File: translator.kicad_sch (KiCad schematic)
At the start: 1 part, among them U1 STM32G071K8UxN

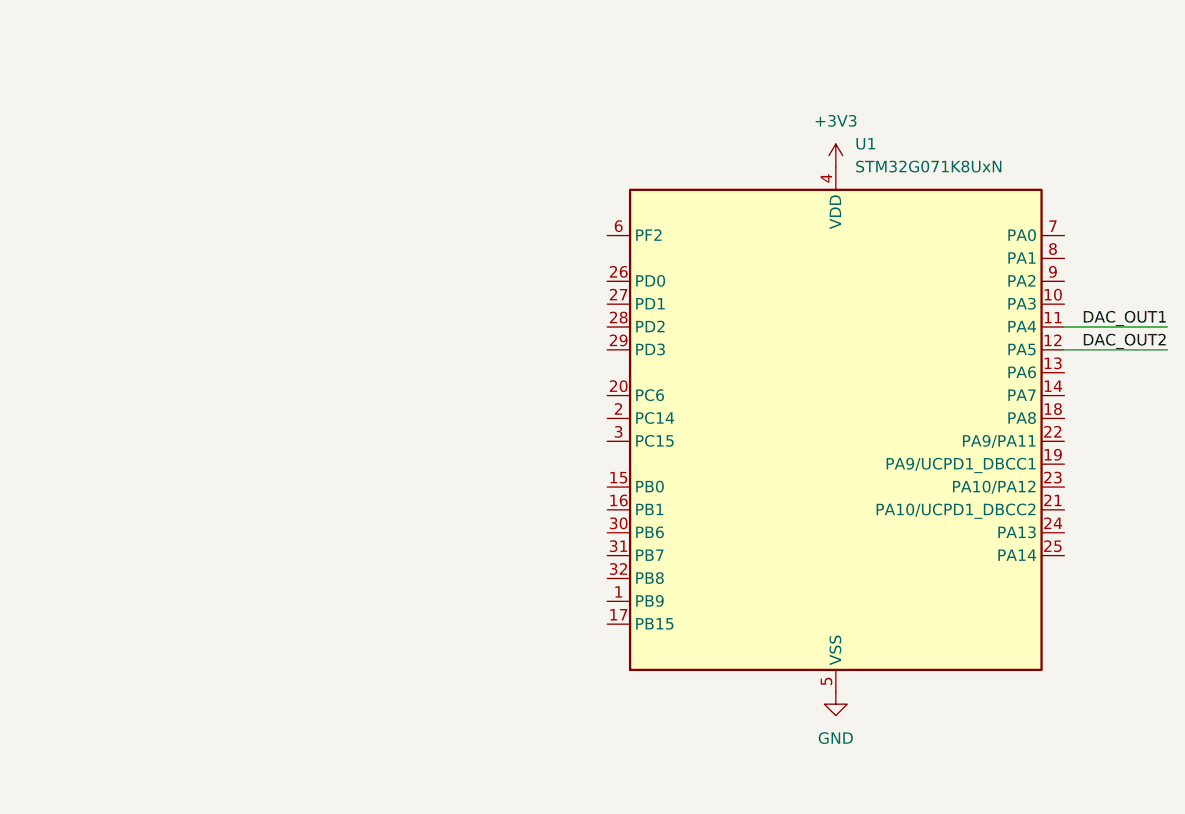
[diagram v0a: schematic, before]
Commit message: add schematic and pedal pinout
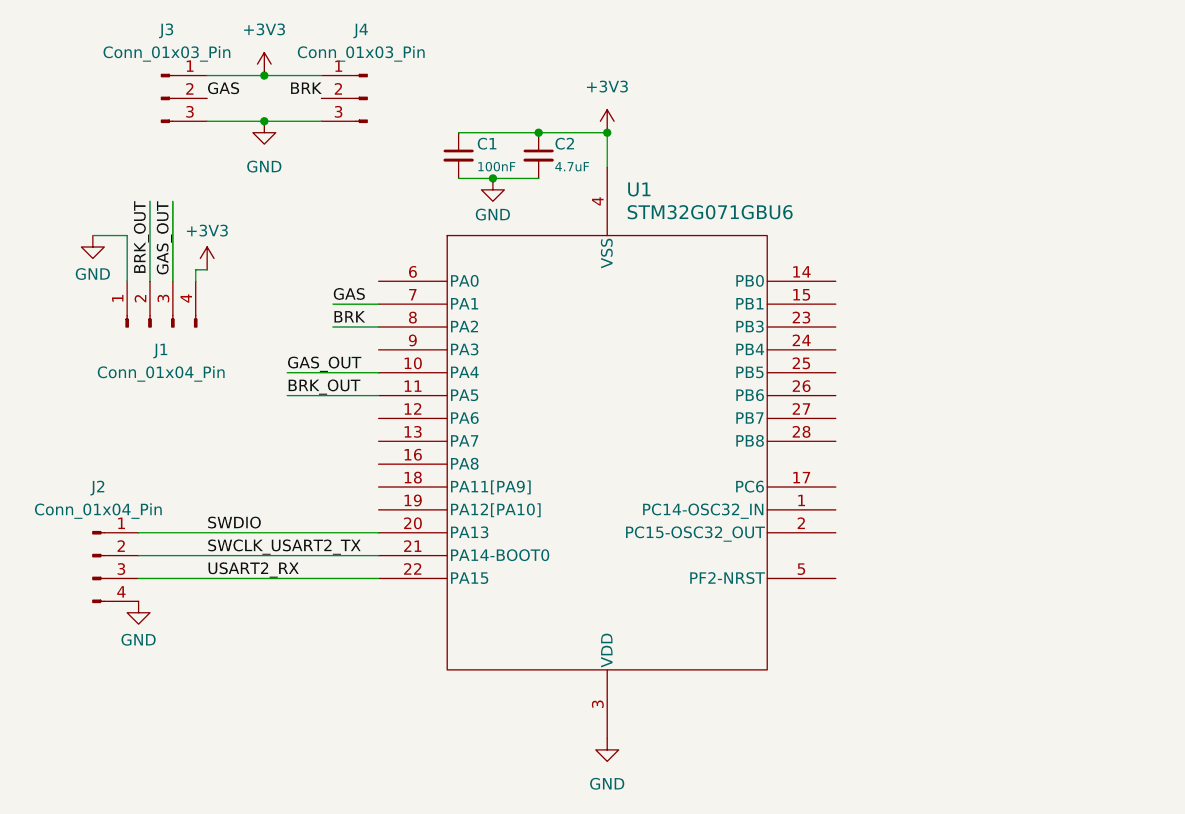
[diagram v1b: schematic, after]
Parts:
- removed U1: STM32G071K8UxN, Package_DFN_QFN:QFN-32-1EP_5x5mm_P0.5mm_EP3.45x3.45mm, symbol MCU_ST_STM32G0:STM32G071K8UxN
- added C1: 100nF, symbol Device:C_Small
- added C2: 4.7uF, symbol Device:C_Small
- added J1, J2: Conn_01x04_Pin, symbol Connector:Conn_01x04_Pin
- added J3, J4: Conn_01x03_Pin, symbol Connector:Conn_01x03_Pin
- added U1: STM32G071GBU6, translator:UFQFPN-28, symbol translator:STM32G071GBU6
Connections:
- net +3V3: now also C1.1, C2.1, J1.4 (Pin_4), J3.1 (Pin_1), J4.1 (Pin_1), U1.4 (VSS)
- net GND: now also C1.2, C2.2, J1.1 (Pin_1), J2.4 (Pin_4), J3.3 (Pin_3), J4.3 (Pin_3), U1.3 (VDD)
- new net BRK: J4.2 (Pin_2), U1.8 (PA2)
- new net BRK_OUT: J1.2 (Pin_2), U1.11 (PA5)
- new net GAS: J3.2 (Pin_2), U1.7 (PA1)
- new net GAS_OUT: J1.3 (Pin_3), U1.10 (PA4)
- new net SWCLK_USART2_TX: J2.2 (Pin_2), U1.21 (PA14-BOOT0)
- new net SWDIO: J2.1 (Pin_1), U1.20 (PA13)
- new net USART2_RX: J2.3 (Pin_3), U1.22 (PA15)
